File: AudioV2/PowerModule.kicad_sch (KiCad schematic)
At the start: 9 parts, among them J1 USB-C PD in, J202 +12/-12/A_GND, U1 DKMW20F-12, U2 50224_CH224, U3 LM7809 +9V

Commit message: fix(AudioV2): PowerModule を §9 どおり簡素配線に修正
- USB-C VBUS/GND → CH224、12V → PD_12V/J_PD（SW前）
- PD_12V_SW → F1 → DKMW +Vin、PD_GND を -Vin/R.C. に一本化
- ±12V/A_GND → J202、+12V → LM7809 → VCC_TONE
- C101/C102/C103/C104 と 7809 デカップ追加
- ピン座標ヘルパで F1(rot90)/7809/コネクタを正しく接続
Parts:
- added C101, C102, C103: 47u, symbol Device:C
- added C104: 0.1u, symbol Device:C
- J202: value +12/-12/A_GND -> +12/-12/A_GND out
- J_PD: value PD_12V to panel -> PD_12V/GND to panel
- U2: value 50224_CH224 -> 50224_CH224 12V
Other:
- note added: "AudioV2 PowerModule — simplified wired (§9 / CIRCUIT_DESIGN §4) USB-C → 50224 CH224 → PD_12V/J_PD → (panel SW) → PD_12V_SW → F1 → DKMW20F-12 ±12V + A_GND → J202 / hier. LM7809 → VCC_TONE (+9V). Bench +12V_IN: TBD."
- note removed: "AudioV2 PowerModule — CIRCUIT_DESIGN wired U1 DKMW20F-12 / U2 50224 / F1 3A slow / U3 LM7809 +9V See CIRCUIT_DESIGN.md §4"

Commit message: AudioV2 PowerModule: embed lib_symbols and fix KiCad 10 symbol instances
PowerModule was showing pads-only in KiCad Viewer because lib_symbols was
empty and symbol instances lacked KiCad 10 pin UUID blocks.

- Add sch_helpers.py: embed_lib_symbols, symbol_inst_v10, pin_connect
- Regenerate PowerModule with embedded standard/custom symbol graphics
- Use Connector:USB_C_Receptacle_USB2.0_16P with correct A1/A4/… pin IDs
- Wire from computed pin tips with schematic Y-axis flip
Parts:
- removed J1: USB-C PD in, symbol Connector:USB_C_Receptacle_USB2.0
- added J1: USB-C PD in, symbol Connector:USB_C_Receptacle_USB2.0_16P
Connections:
- new net: J1.A1 (GND), J1.A12 (GND), J1.B1 (GND), J1.B12 (GND)
- new net: J1.A4 (VBUS), J1.A9 (VBUS), J1.B4 (VBUS), J1.B9 (VBUS)

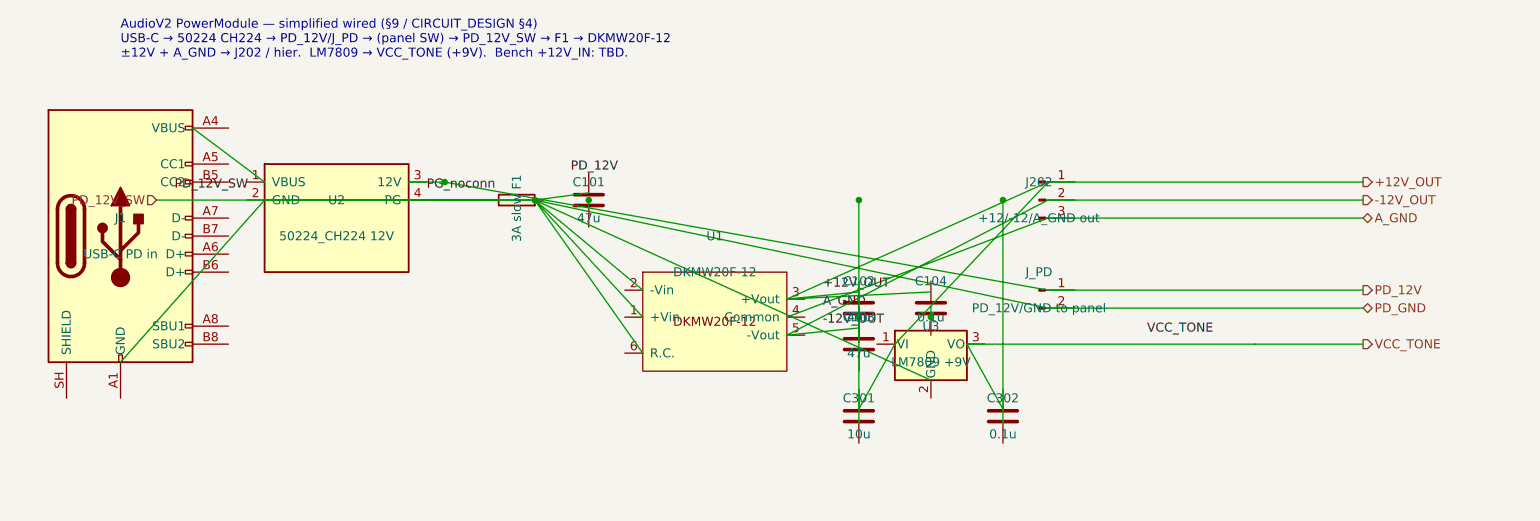
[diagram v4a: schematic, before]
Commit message: fix(AudioV2): WP-B embed flatten / OLED / PowerModule 一次二次分離
WP-A A1/A2 も取り込み: AudioV2.kicad_sym の二重 embedded_fonts 除去と
PT2314 float 座標正規化。embed_lib_symbols は extends を親ピン付き定義へ
flatten。OLED は Conn_01x04 ヘッダに置換。PowerModule は PD_GND と
PD_12V_SW/F1 の Y 衝突を解消し、7809 GND→A_GND、R.C. オープン。

Co-authored-by: m_arino <indare@users.noreply.github.com>
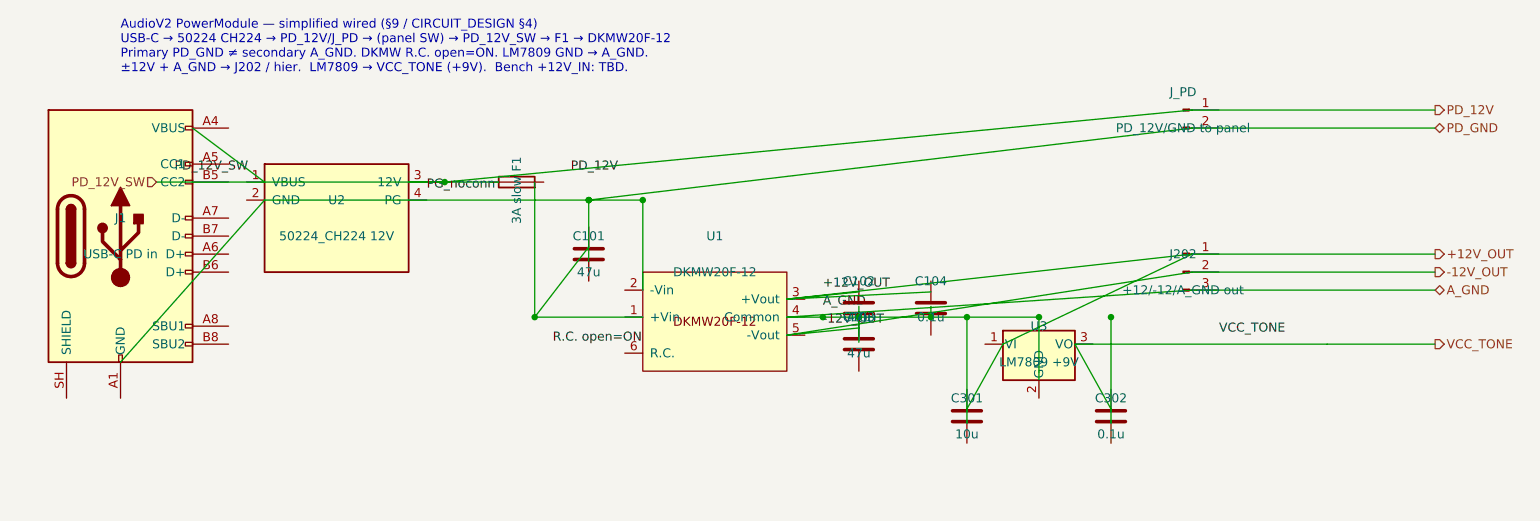
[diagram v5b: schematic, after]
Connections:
- net A_GND: now also C103.1
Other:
- note added: "AudioV2 PowerModule — simplified wired (§9 / CIRCUIT_DESIGN §4) USB-C → 50224 CH224 → PD_12V/J_PD → (panel SW) → PD_12V_SW → F1 → DKMW20F-12 Primary PD_GND ≠ secondary A_GND. DKMW R.C. open=ON. LM7809 GND → A_GND. ±12V + A_GND → J202 / hier. LM7809 → VCC_TONE (+9V). Bench +12V_IN: TBD."
- note removed: "AudioV2 PowerModule — simplified wired (§9 / CIRCUIT_DESIGN §4) USB-C → 50224 CH224 → PD_12V/J_PD → (panel SW) → PD_12V_SW → F1 → DKMW20F-12 ±12V + A_GND → J202 / hier. LM7809 → VCC_TONE (+9V). Bench +12V_IN: TBD."

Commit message: AudioV2: ラベル結線で Power/Control/Output をネット接続
pin_connect を tip=(at) 基準に修正し、同名ローカルラベルをピン tip に
載せて結線。グリッドスナップ一致・パッシブ間隔・親シートピン橋渡しを
整え、一次 PD_GND と二次 A_GND の分離を維持。
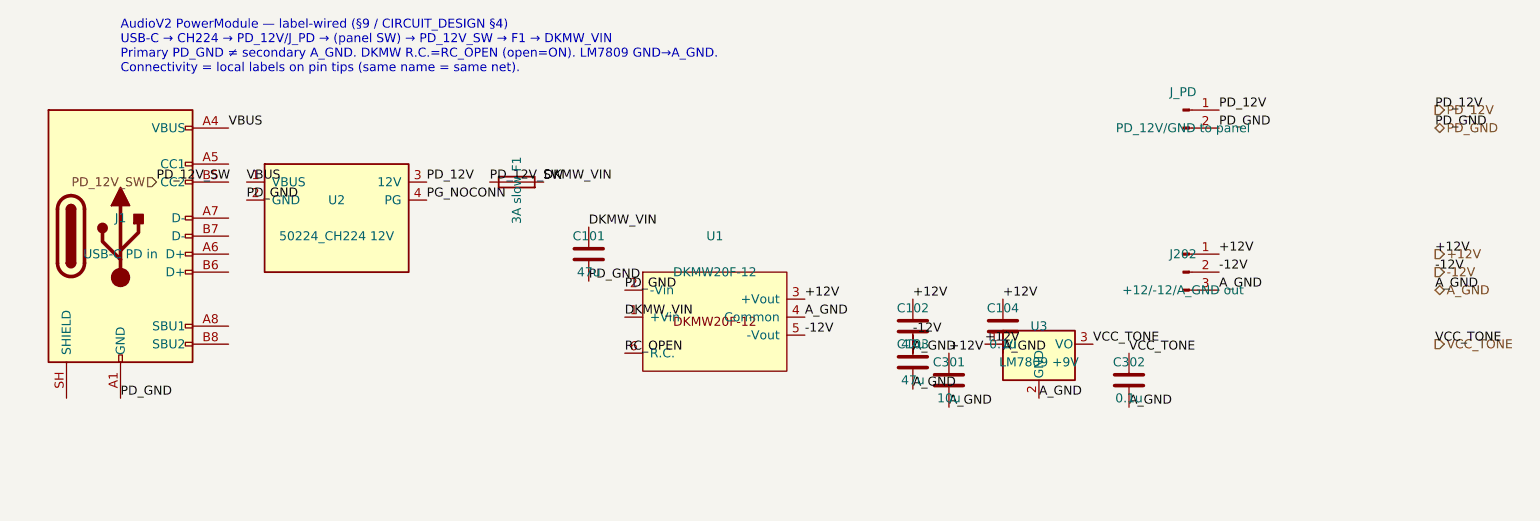
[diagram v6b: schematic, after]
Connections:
- net A_GND: now also C102.2, C103.2, C104.2, C301.2, C302.2, J202.3 (Pin_3), U1.4 (Common), U3.2 (GND); no longer C103.1
- net PD_12V: now also J_PD.1 (Pin_1), U2.3 (12V)
- net PD_GND: now also C101.2, J1.A1 (GND), J1.A12 (GND), J1.B1 (GND), J1.B12 (GND), J_PD.2 (Pin_2), U1.2 (-Vin), U2.2 (GND)
- net VCC_TONE: now also C302.1, U3.3 (VO)
- net +12V: now reaches C301.1
- net +12V: now also C102.1, C104.1, J202.1 (Pin_1), U1.3 (+Vout), U3.1 (VI)
- net DKMW_VIN: now reaches C101.1
- net DKMW_VIN: now also F1.2, U1.1 (+Vin)
- net VBUS: now reaches U2.1 (VBUS)
- net VBUS: now also J1.A4 (VBUS), J1.A9 (VBUS), J1.B4 (VBUS), J1.B9 (VBUS)
- net PG_NOCONN: now reaches U2.4 (PG)
- net -12V: now reaches J202.2 (Pin_2)
- net -12V: now also C103.1, U1.5 (-Vout)
- net RC_OPEN: now reaches U1.6 (R.C.)
- net PD_12V_SW: now reaches F1.1
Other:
- note added: "AudioV2 PowerModule — label-wired (§9 / CIRCUIT_DESIGN §4) USB-C → CH224 → PD_12V/J_PD → (panel SW) → PD_12V_SW → F1 → DKMW_VIN Primary PD_GND ≠ secondary A_GND. DKMW R.C.=RC_OPEN (open=ON). LM7809 GND→A_GND. Connectivity = local labels on pin tips (same name = same net)."
- note removed: "AudioV2 PowerModule — simplified wired (§9 / CIRCUIT_DESIGN §4) USB-C → 50224 CH224 → PD_12V/J_PD → (panel SW) → PD_12V_SW → F1 → DKMW20F-12 Primary PD_GND ≠ secondary A_GND. DKMW R.C. open=ON. LM7809 GND → A_GND. ±12V + A_GND → J202 / hier. LM7809 → VCC_TONE (+9V). Bench +12V_IN: TBD."
